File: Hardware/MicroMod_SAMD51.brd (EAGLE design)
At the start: 22 x 22 mm, 35 parts, among them J2 MICROMOD-2222, U1 W25QXX6X5, U2 ATSAMD51J20A-A, Y1 32.768kHz

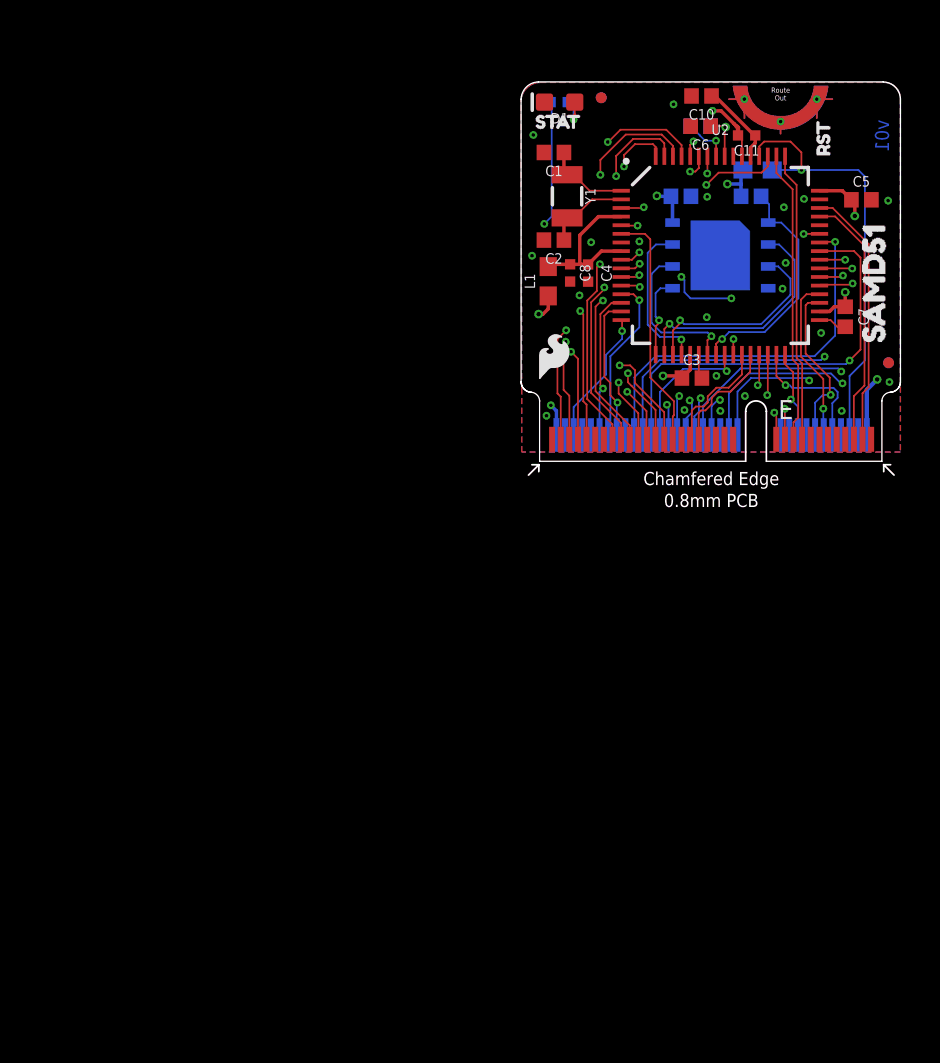
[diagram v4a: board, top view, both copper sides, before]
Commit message: Updates symobl for SAMD51 to latest
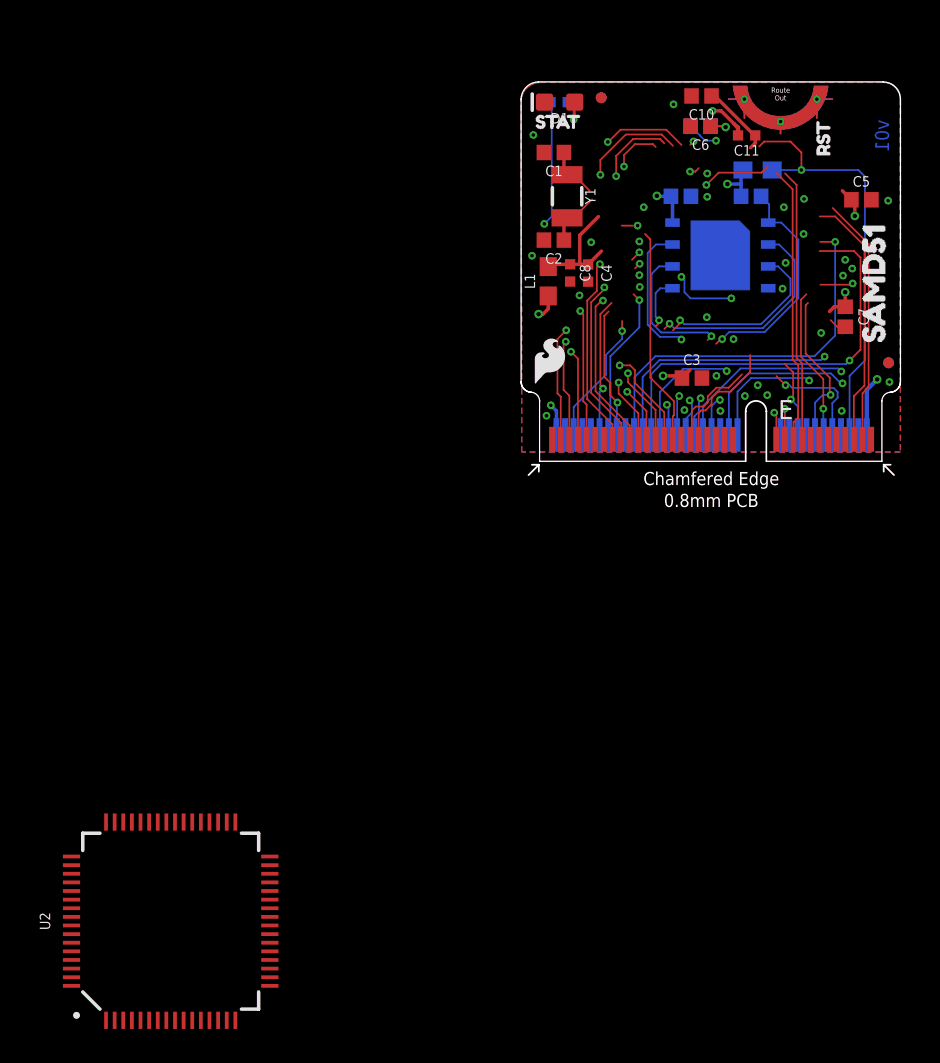
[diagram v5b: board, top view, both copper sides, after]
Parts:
- moved U2 50.1 mm to (-20.3, -26.7), turned to 0 degrees
- moved U$7 0.36 mm to (1.65, 5.84)
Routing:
- net 3.3V: track 23.3 -> 18.8 mm
- net GND: track 6.72 -> 3.91 mm
- net VDDA: track 9.15 -> 6.68 mm
- net SDA1: track 14.0 -> 11.6 mm
- net D8: track 27.0 -> 25.2 mm
- net XIN32: track 4.89 -> 3.06 mm
- net SCL1: track 13.7 -> 12.0 mm
- net XOUT32: track 4.95 -> 3.26 mm
- net QSPI_DAT0: track 4.83 -> 3.19 mm
- net D7: track 27.0 -> 25.5 mm
- net QSPI_DAT1: track 14.0 -> 12.6 mm
- net QSPI_DAT2: track 11.9 -> 10.5 mm
- net A3/PWM1: track 14.0 -> 12.6 mm
- net D3: track 18.2 -> 16.9 mm
- net A0: track 31.0 -> 29.7 mm
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
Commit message: Updates Design
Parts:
- removed U$9: (no value), reset:RST0
- R1: device SparkFun-Resistors:0603 -> SparkFun-Resistors:0402-TIGHT
- U1: value W25QXX6X5 -> W25QXX128MBIT-6X5-NO_CENTER; device SparkFun-MicroMod:WSON-8-6X5 -> SparkFun-MicroMod:WSON-8-6X5-NO_CENTERPAD
- moved U2 50.1 mm to (11.7, 11.8), turned to 270 degrees
- moved LOGO2 23.2 mm to (19.8, 20.2)
- moved LOGO6 10.1 mm to (9.16, 6.84)
- moved U$5 5.16 mm to (10.7, 4.86)
- moved U$4 4.68 mm to (20.7, 4.86)
- moved U$7 0.60 mm to (1.90, 6.39)
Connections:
- removed net 3.3V_EN: J2.4
- net A1: now also U2.6; no longer U2.11
- net A3/PWM1: now also U2.11; no longer U2.6
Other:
- outline, holes or cut-outs redrawn

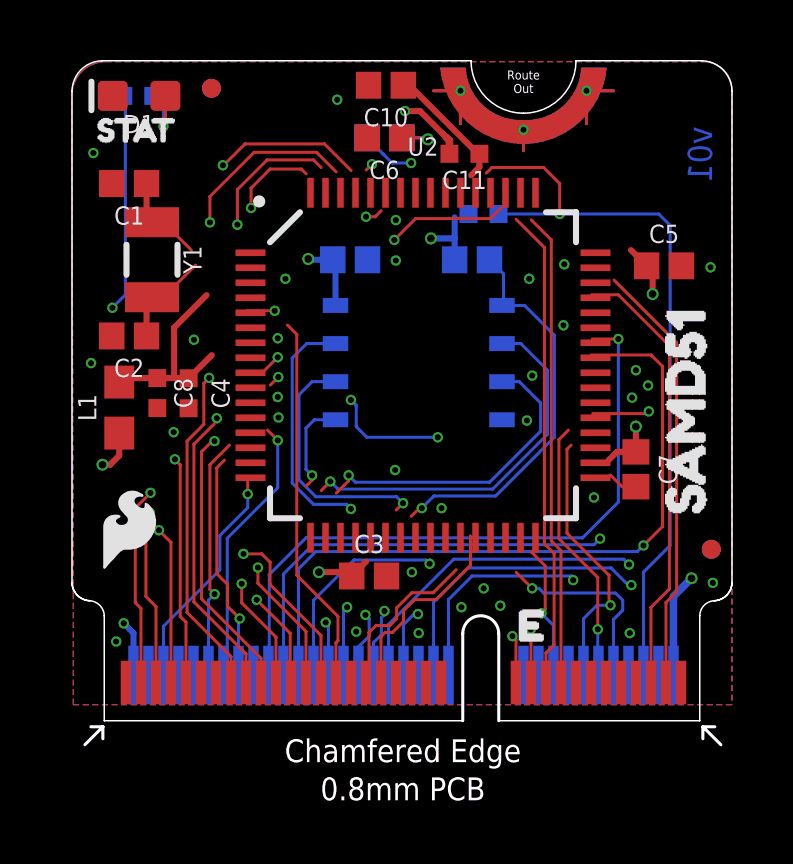
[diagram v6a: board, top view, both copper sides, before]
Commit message: Changes Ferrite bead to 0402, completes trace work since symbol for SAMD51 was recreated
* Changes all parts to 0402 tight and fixes traces accordingly
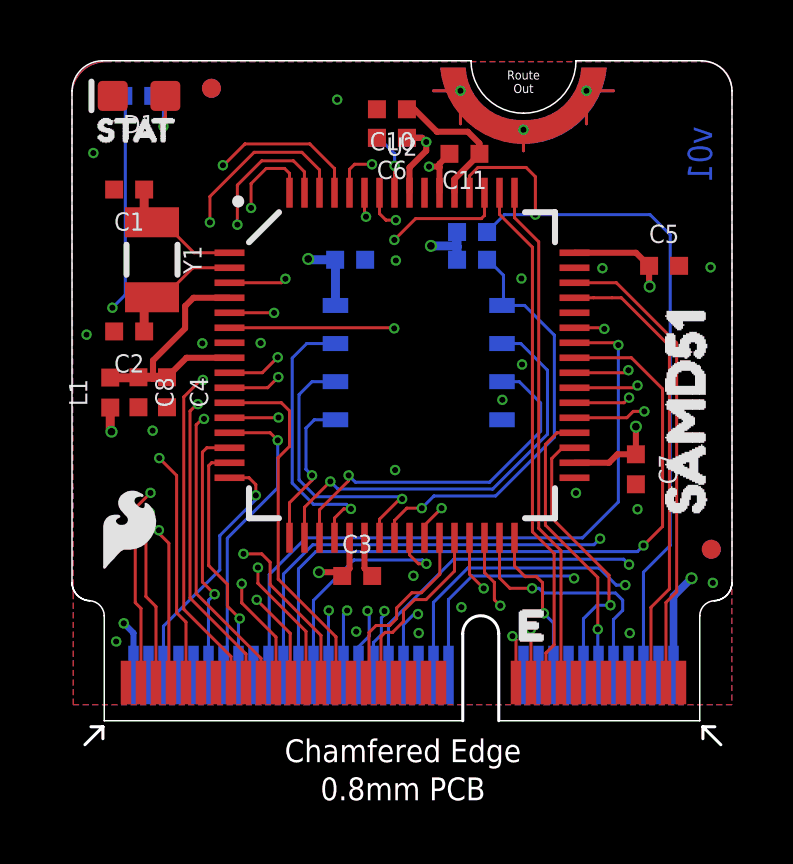
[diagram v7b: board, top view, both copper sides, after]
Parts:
- C1, C10, C2, C3, C5, C6, C7, C9: device SparkFun-Capacitors:0402 -> SparkFun-Capacitors:0402-TIGHT
- L1: value (none) -> 30Ω; device SparkFun-Coils:0603 -> SparkFun-Coils:0402-TIGHT
- R2: value 1K -> 1k; device SparkFun-Resistors:0402 -> SparkFun-Resistors:0402-TIGHT
- R4: value 100K -> 100k; device SparkFun-Resistors:0402 -> SparkFun-Resistors:0402-TIGHT
- moved C10 0.82 mm to (10.7, 20.4)
- moved C4 0.72 mm to (3.17, 10.9)
- moved R1 0.71 mm to (13.3, 16.3)
- moved U2 0.70 mm to (11.0, 11.8)
- moved C8 0.63 mm to (2.21, 10.9)
- moved L1 0.58 mm to (1.27, 10.9)
- moved C3 0.40 mm to (9.51, 4.83)
- moved C6 0.25 mm to (10.7, 19.4)
- moved R2 0.25 mm to (10.7, 19.4)
- moved C1 0.20 mm to (1.91, 17.7)
- moved C2 0.15 mm to (1.91, 13.0)
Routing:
- net D7: track 25.5 -> 19.4 mm
- net 3.3V: track 18.7 -> 22.4 mm
- net A1: track 15.8 -> 19.0 mm, vias 4 -> 2
- net SDA1: track 11.6 -> 14.1 mm
- net D10: track 13.9 -> 16.1 mm
- net VDDA: track 6.68 -> 8.70 mm
- net A2/PWM0: track 23.8 -> 25.8 mm
- net QSPI_DAT0: track 3.19 -> 5.15 mm
- net D0: track 6.55 -> 8.37 mm
- net QSPI_DAT1: track 12.6 -> 14.4 mm
- net D8: track 25.2 -> 26.9 mm
- net SCL1: track 12.0 -> 13.8 mm
- net QSPI_DAT2: track 10.5 -> 12.2 mm
- net D3: track 16.9 -> 18.6 mm
- net A0: track 29.7 -> 31.3 mm
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
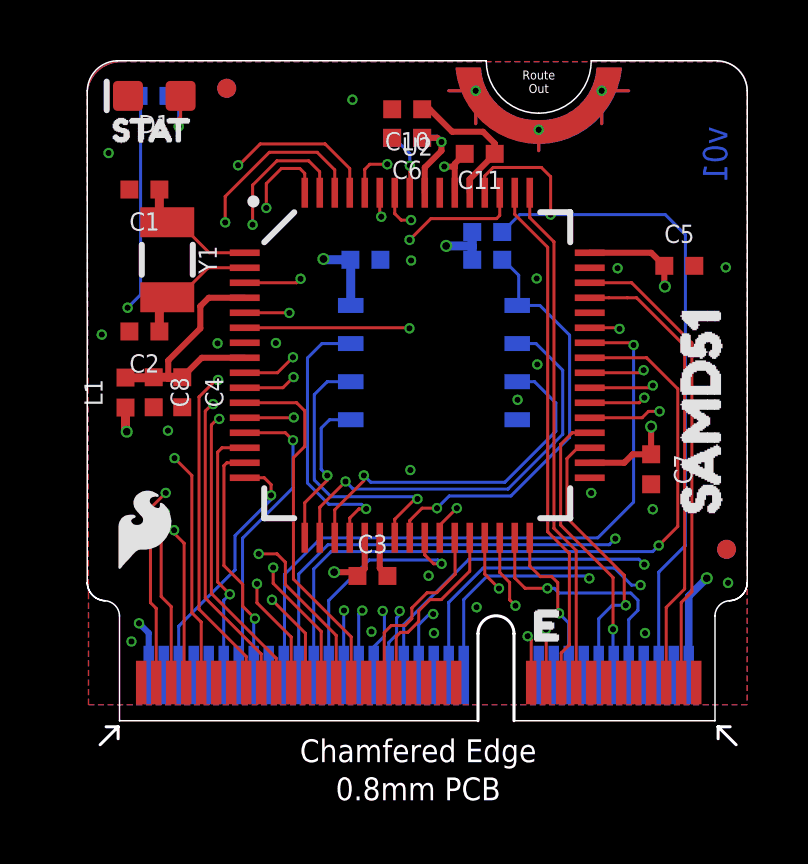
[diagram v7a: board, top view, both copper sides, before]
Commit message: Adds Differential ADC lines, battery voltage connection, 3.3V enable line
* Also adds diode to prevent backpowering 3.3V line from RTC_3V
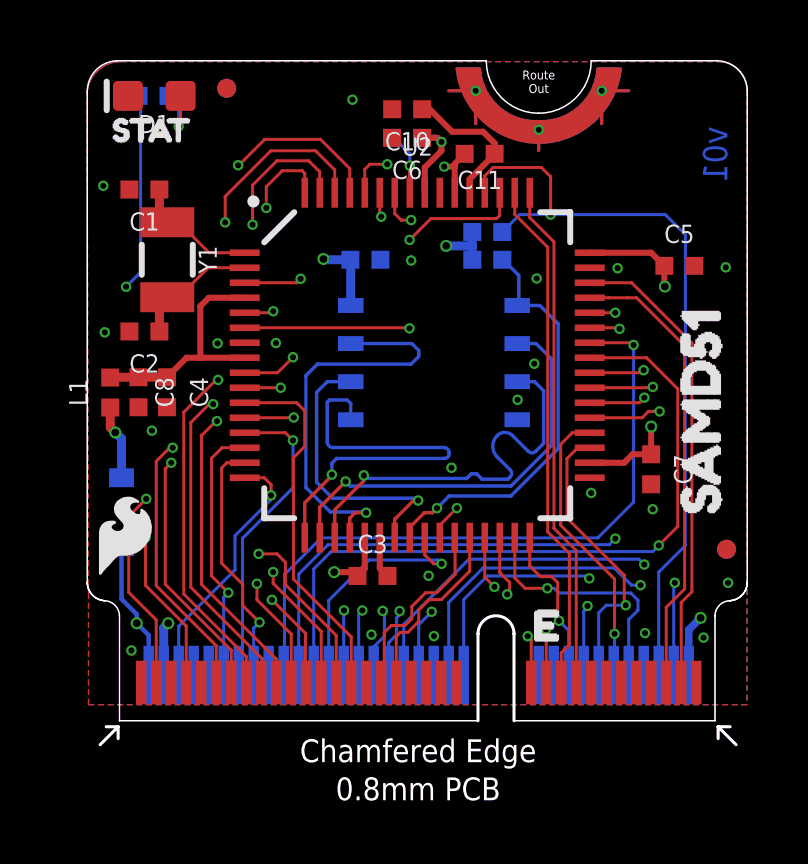
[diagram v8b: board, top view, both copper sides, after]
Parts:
- added D3: 1A/23V/620mV, SparkFun-DiscreteSemi:SOD-323
- moved U$7 0.68 mm to (1.25, 6.19)
- moved C4 0.51 mm to (2.66, 10.9)
- moved L1 0.51 mm to (0.77, 10.9)
- moved C8 0.51 mm to (1.71, 10.9)
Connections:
- removed net !INT: J2.16
- removed net D10: J2.67, U2.10
- removed net D8: J2.71, U2.39
- removed net D9: J2.69, U2.26
- new net 3.3V_EN: J2.4, U2.39
- new net 3.3V_IN: D3.A, J2.2, J2.74
- new net A5: J2.65, U2.5
- new net A6: J2.63, U2.10
- new net D8/!INT: J2.16, J2.69, U2.26
- net 3.3V: now also D3.C, J2.72; no longer J2.2, J2.74
- net D13: now also U2.44; no longer U2.5
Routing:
- net 3.3V_IN: track 0.00 -> 27.9 mm, vias 0 -> 2
- net D8: track 26.9 -> 0.00 mm, vias 2 -> 0
- net D8/!INT: track 0.00 -> 25.5 mm, vias 0 -> 3
- net A5: track 0.00 -> 17.2 mm, vias 0 -> 2
- net D9: track 16.3 -> 0.00 mm, vias 2 -> 0
- net D10: track 16.1 -> 0.00 mm, vias 2 -> 0
- net A6: track 0.00 -> 15.1 mm, vias 0 -> 2
- net 3.3V_EN: track 0.00 -> 12.0 mm, vias 0 -> 2
- net D13: track 14.2 -> 24.1 mm
- net QSPI_DAT0: track 5.15 -> 13.9 mm
- net D7: track 19.4 -> 27.9 mm
- net QSPI_DAT3: track 9.46 -> 14.0 mm
- net 3.3V: track 22.4 -> 20.5 mm, vias 9 -> 8
- net QSPI_DAT2: track 12.2 -> 13.8 mm
- net SDA1: track 14.1 -> 13.3 mm
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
